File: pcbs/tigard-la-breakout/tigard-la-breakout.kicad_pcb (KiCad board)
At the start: 2 copper layers, 32.2 x 28.2 mm, 3 parts, among them J1 Tigard, J2 FX2, J3 Saleae

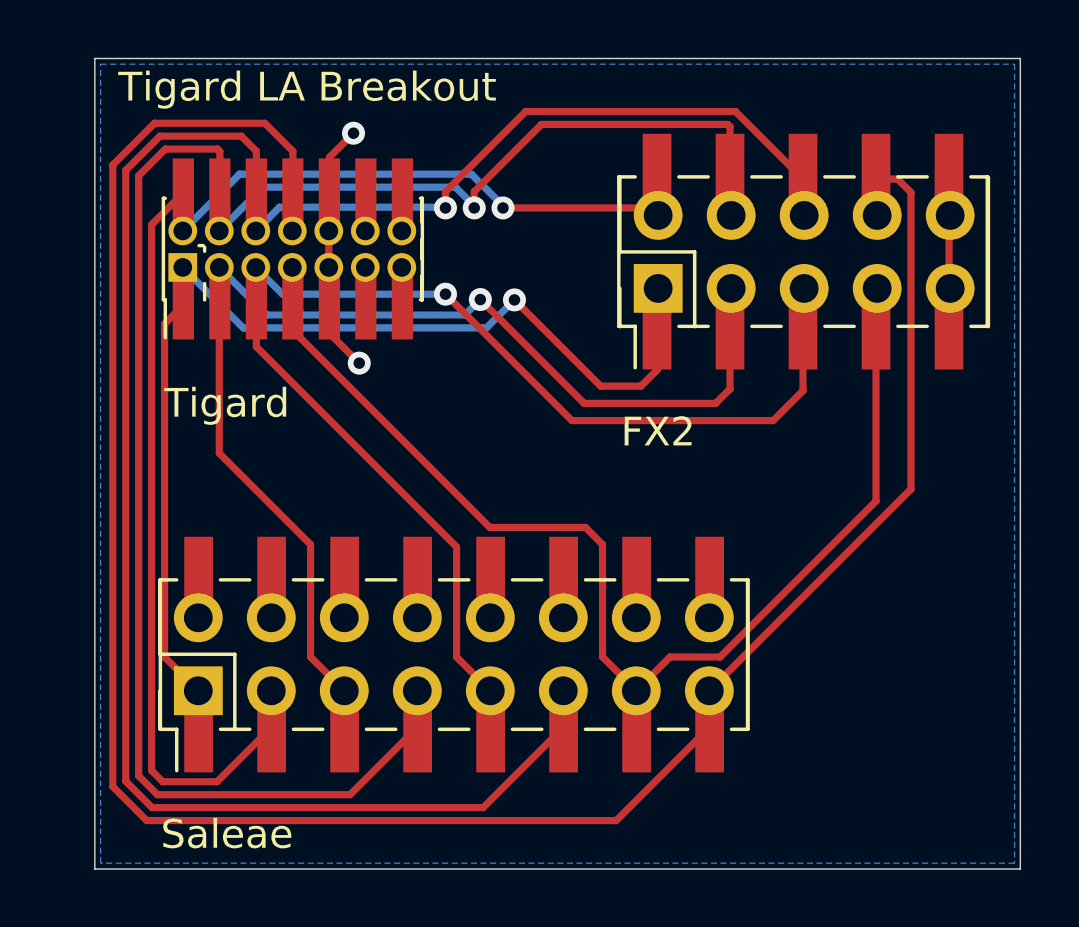
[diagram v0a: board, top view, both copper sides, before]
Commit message: Add silkscreen
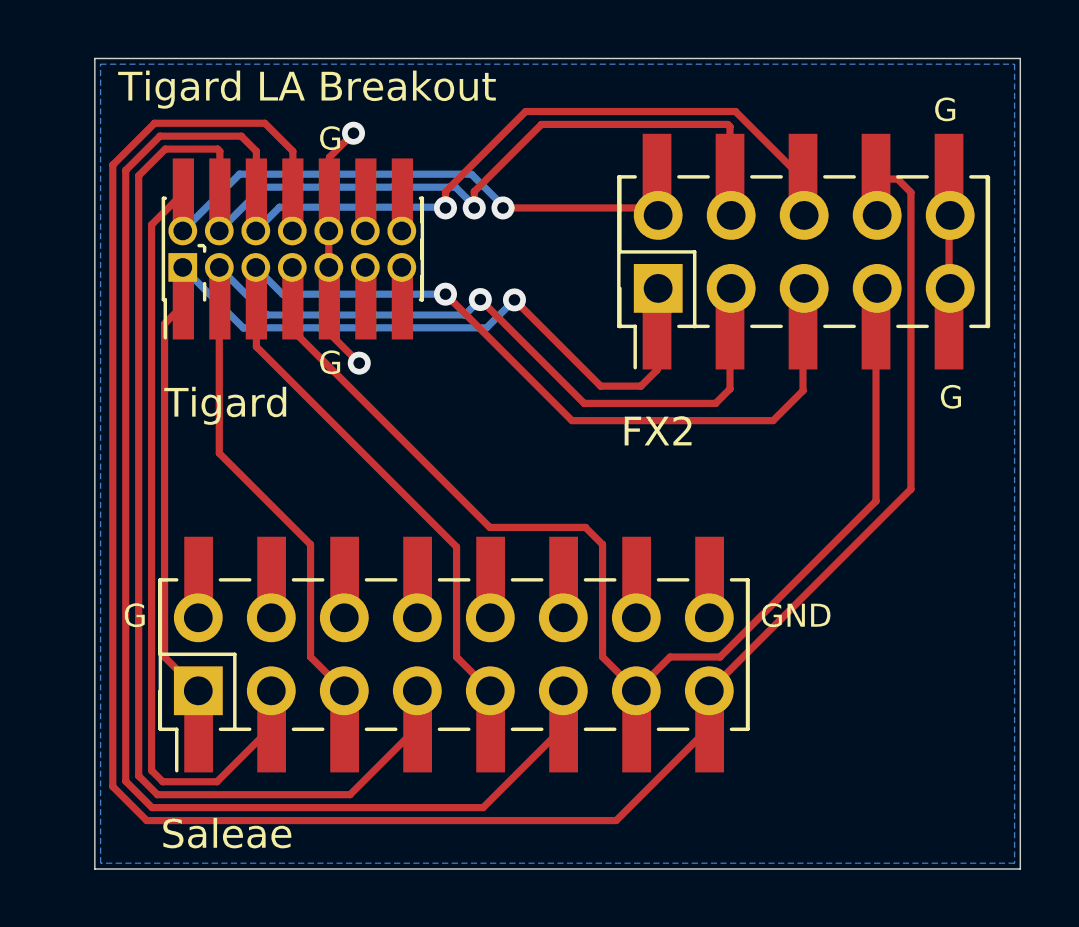
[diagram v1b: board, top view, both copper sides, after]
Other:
- board text added: "G"
- board text added: "GND"
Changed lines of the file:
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@@
   (general
     (thickness 1.6)
-    (drawings 5)
+    (drawings 11)
     (tracks 154)
     (zones 0)
@@
       (outputformat 1)
       (mirror false)
-      (drillshape 1)
+      (drillshape 0)
       (scaleselection 1)
-      (outputdirectory ""))
+      (outputdirectory "output/"))
   )
   (net 0 "")
@@
       (net 3 /CH2))
   )
+  (gr_text G (at 142.8 59.4) (layer F.SilkS)
+    (effects (font (size 0.8 0.8) (thickness 0.15)))
+  )
+  (gr_text GND (at 165.8 59.4) (layer F.SilkS)
+    (effects (font (size 0.8 0.8) (thickness 0.15)))
+  )
+  (gr_text G (at 171 41.8) (layer F.SilkS)
+    (effects (font (size 0.8 0.8) (thickness 0.15)))
+  )
+  (gr_text G (at 171.2 51.8) (layer F.SilkS)
+    (effects (font (size 0.8 0.8) (thickness 0.15)))
+  )
+  (gr_text G (at 149.6 50.6) (layer F.SilkS)
+    (effects (font (size 0.8 0.8) (thickness 0.15)))
+  )
+  (gr_text G (at 149.6 42.8) (layer F.SilkS)
+    (effects (font (size 0.8 0.8) (thickness 0.15)))
+  )
   (gr_text "Tigard LA Breakout" (at 148.8 41) (layer F.SilkS)
